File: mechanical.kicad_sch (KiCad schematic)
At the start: 13 parts

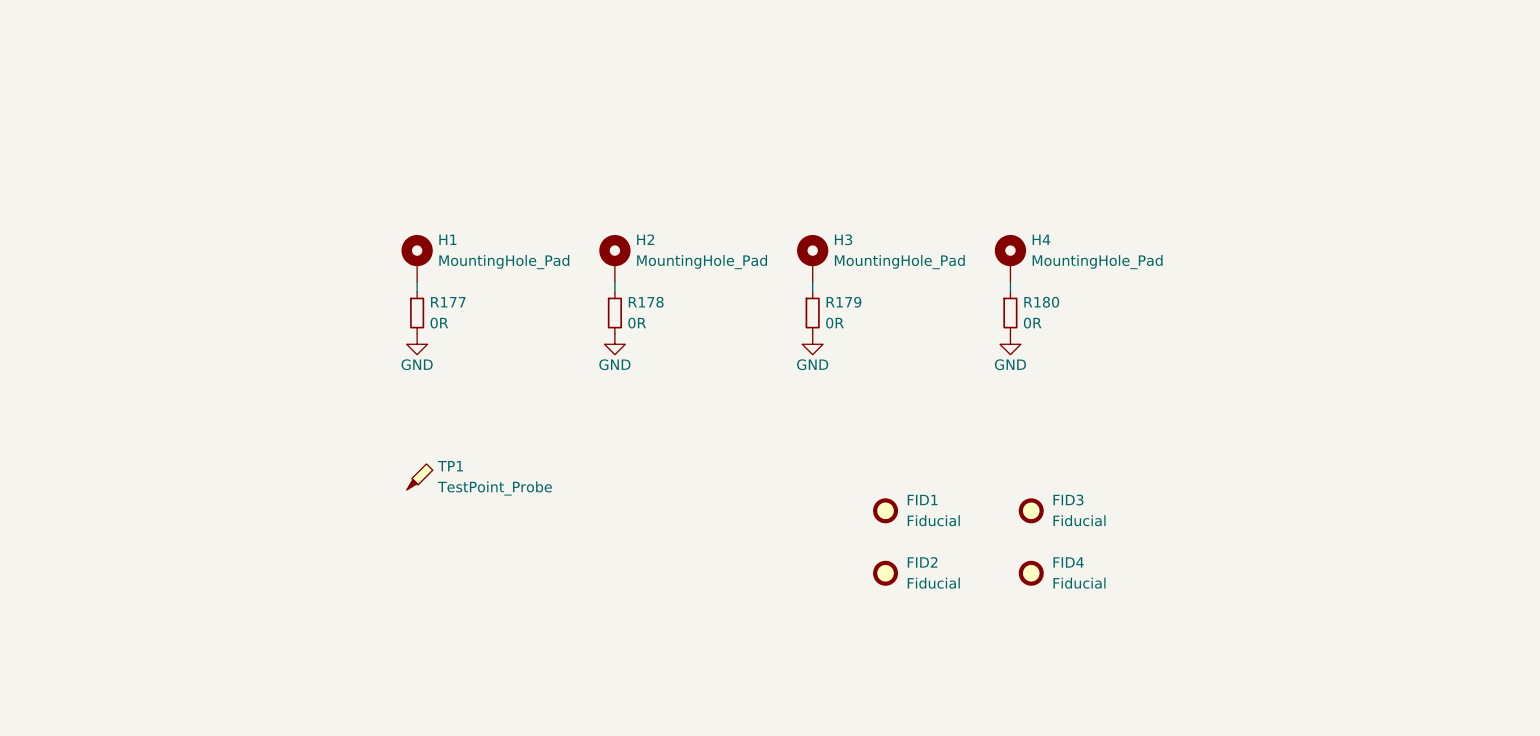
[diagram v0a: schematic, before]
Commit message: SBC Board V0.2
The SBC schematics before footprint and part number check
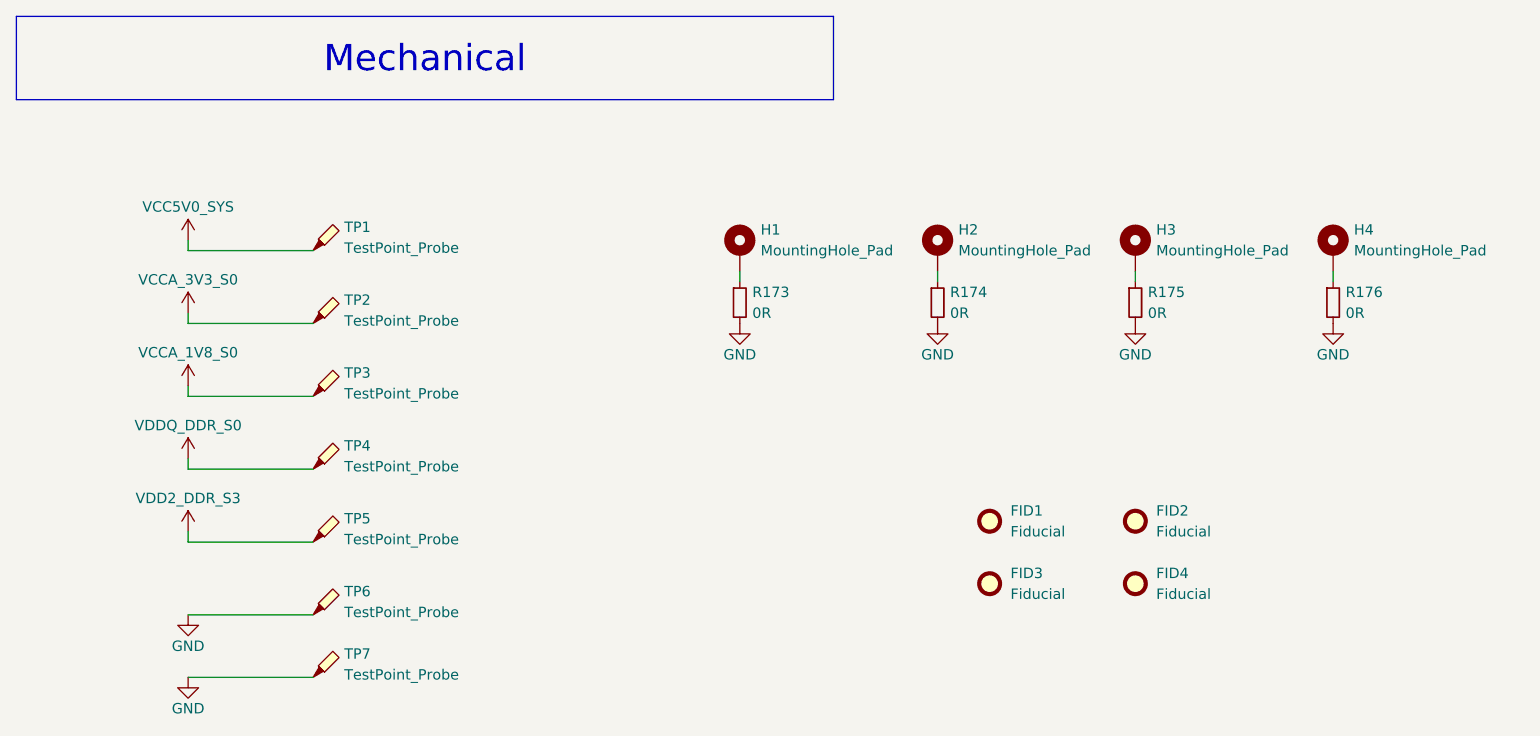
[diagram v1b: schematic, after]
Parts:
- added TP2, TP3, TP4, TP5, TP6, TP7: TestPoint_Probe, symbol Connector:TestPoint_Probe
- renumbered FID3 to FID2, FID2 to FID3, R177 to R173, R178 to R174, R179 to R175, R180 to R176
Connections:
- net GND: now also TP6.1, TP7.1
- net VCC5V0_SYS: now reaches TP1.1
- new net VCCA_1V8_S0: TP3.1
- new net VCCA_3V3_S0: TP2.1
- new net VDD2_DDR_S3: TP5.1
- new net VDDQ_DDR_S0: TP4.1
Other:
- moved on the sheet: FID1, FID2, FID3, FID4, H1, H2, H3, H4, R173, R174, R175, R176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

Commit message: SBCv0.3
there is no big thing update just some LCSC & Mouser parts
and Big problem deleted alot of component values (:
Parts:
- FID1, FID2, FID3, FID4: value Fiducial -> (none)
- H1, H2, H3, H4: value MountingHole_Pad -> (none); footprint (none) -> MountingHole:MountingHole_2.7mm_M2.5_DIN965_Pad_TopOnly
- R173, R174, R175, R176: value 0R -> (none); LCSC Part (none) -> (effects
- TP1, TP2, TP3, TP4, TP5, TP6, TP7: value TestPoint_Probe -> (none); Mouser Part (none) -> (stroke (width 0.3048) (type default))

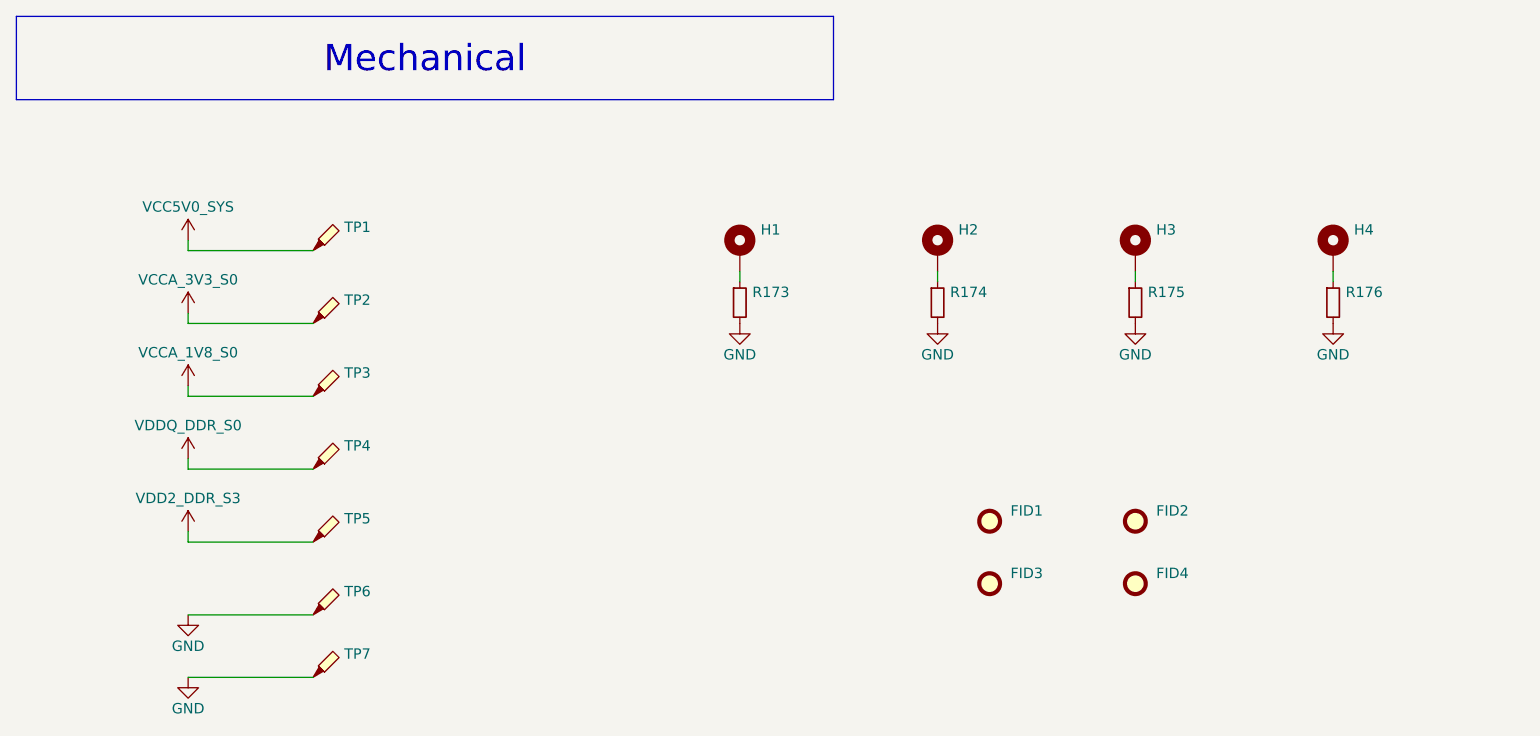
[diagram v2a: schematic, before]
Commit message: SBCv0.4
add LCSC & Mouser parts 
and solve the deleted value in the past version
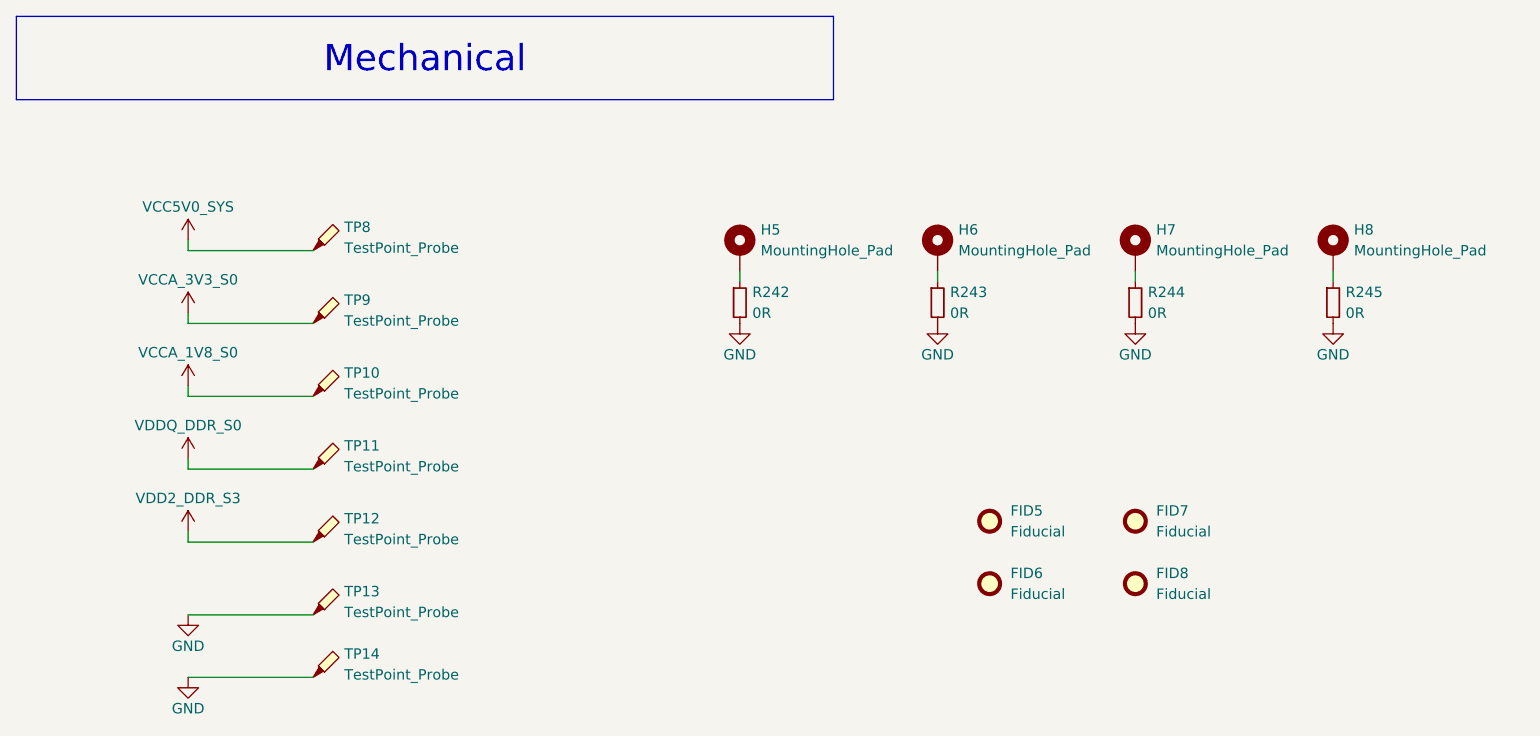
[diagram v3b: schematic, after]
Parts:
- removed FID1, FID2, FID3, FID4: (no value), Fiducial:Fiducial_0.5mm_Mask1.5mm, symbol Mechanical:Fiducial
- removed H1, H2, H3, H4: (no value), MountingHole:MountingHole_2.7mm_M2.5_DIN965_Pad_TopOnly, symbol Mechanical:MountingHole_Pad
- removed R173, R174, R175, R176: (no value), PCM_Resistor_SMD_AKL:R_0402_1005Metric, symbol Device:R_Small
- removed TP1, TP2, TP3, TP4, TP5, TP6, TP7: (no value), symbol Connector:TestPoint_Probe
- added FID5, FID6, FID7, FID8: Fiducial, Fiducial:Fiducial_0.5mm_Mask1.5mm, symbol Mechanical:Fiducial
- added H5, H6, H7, H8: MountingHole_Pad, symbol Mechanical:MountingHole_Pad
- added R242, R243, R244, R245: 0R, PCM_Resistor_SMD_AKL:R_0402_1005Metric, symbol Device:R_Small
- added TP10, TP11, TP12, TP13, TP14, TP8, TP9: TestPoint_Probe, symbol Connector:TestPoint_Probe
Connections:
- net GND: now also R242.2, R243.2, R244.2, R245.2, TP13.1, TP14.1
- net VCC5V0_SYS: now also TP8.1
- net VCCA_1V8_S0: now also TP10.1
- net VCCA_3V3_S0: now also TP9.1
- net VDD2_DDR_S3: now also TP12.1
- net VDDQ_DDR_S0: now also TP11.1
- new net: H6.1, R243.1
- new net: H8.1, R245.1
- new net: H7.1, R244.1
- new net: H5.1, R242.1

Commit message: SBCv0.5
small update for Josa watch the final version
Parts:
- H5, H6, H7, H8: footprint (none) -> MountingHole:MountingHole_2.2mm_M2_DIN965_Pad_TopBottom
- TP10, TP11, TP12, TP13, TP14, TP8, TP9: footprint (none) -> PCM_SparkFun-Connector:TestPoint-0.5mm
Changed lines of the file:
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@@
 			)
 		)
-		(property "Footprint" ""
+		(property "Footprint" "PCM_SparkFun-Connector:TestPoint-0.5mm"
 			(at 53.34 58.42 0)
 			(hide yes)
@@
 			)
 		)
-		(property "Footprint" ""
+		(property "Footprint" "PCM_SparkFun-Connector:TestPoint-0.5mm"
 			(at 53.34 92.71 0)
 			(hide yes)
@@
 			)
 		)
-		(property "Footprint" ""
+		(property "Footprint" "MountingHole:MountingHole_2.2mm_M2_DIN965_Pad_TopBottom"
 			(at 124.46 40.64 0)
 			(hide yes)
@@
 			)
 		)
-		(property "Footprint" ""
+		(property "Footprint" "MountingHole:MountingHole_2.2mm_M2_DIN965_Pad_TopBottom"
 			(at 148.59 40.64 0)
 			(hide yes)
@@
 			)
 		)
-		(property "Footprint" ""
+		(property "Footprint" "MountingHole:MountingHole_2.2mm_M2_DIN965_Pad_TopBottom"
 			(at 100.33 40.64 0)
 			(hide yes)
@@
 			)
 		)
-		(property "Footprint" ""
+		(property "Footprint" "PCM_SparkFun-Connector:TestPoint-0.5mm"
 			(at 53.34 49.53 0)
 			(hide yes)
@@
 			)
 		)
-		(property "Footprint" ""
+		(property "Footprint" "MountingHole:MountingHole_2.2mm_M2_DIN965_Pad_TopBottom"
 			(at 172.72 40.64 0)
 			(hide yes)
@@
 			)
 		)
-		(property "Footprint" ""
+		(property "Footprint" "PCM_SparkFun-Connector:TestPoint-0.5mm"
 			(at 53.34 40.64 0)
 			(hide yes)
@@
 			)
 		)
-		(property "Footprint" ""
+		(property "Footprint" "PCM_SparkFun-Connector:TestPoint-0.5mm"
 			(at 53.34 76.2 0)
 			(hide yes)
@@
 			)
 		)
-		(property "Footprint" ""
+		(property "Footprint" "PCM_SparkFun-Connector:TestPoint-0.5mm"
 			(at 53.34 67.31 0)
 			(hide yes)
@@
 			)
 		)
-		(property "Footprint" ""
+		(property "Footprint" "PCM_SparkFun-Connector:TestPoint-0.5mm"
 			(at 53.34 85.09 0)
 			(hide yes)
